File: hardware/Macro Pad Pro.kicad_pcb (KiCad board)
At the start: 2 copper layers, 107 x 134 mm, 149 parts, among them J1 USB_C, J2 Conn_02x08_Odd_Even, J4 Conn_02x01, SW1 SW_Push_B, SW2 SW_Push_R, U1 RP2040, U2 OLED, U3 AP2112K-3.3, U4 USBLC6-2SC6, U6 W25Q128JVS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

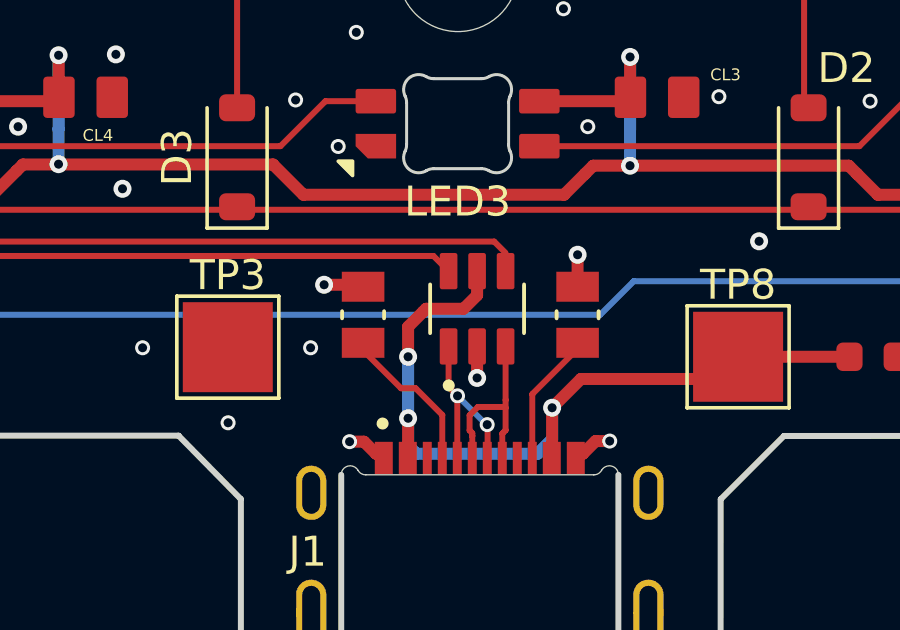
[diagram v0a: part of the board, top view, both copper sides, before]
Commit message: Fixed ERC component footprint
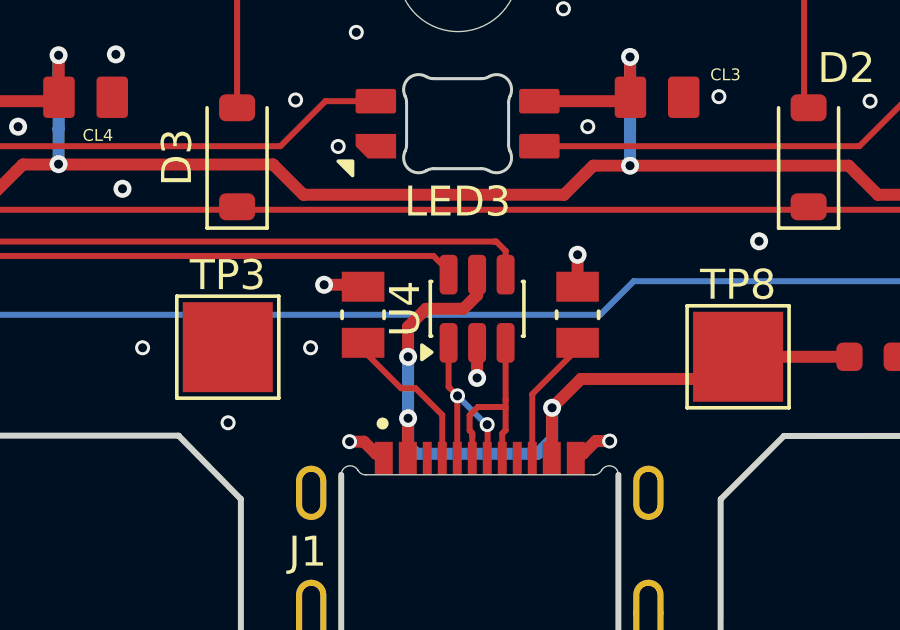
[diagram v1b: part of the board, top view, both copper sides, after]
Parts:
- U4: footprint Personal:SOT95P280X145-6N -> Package_TO_SOT_SMD:SOT-23-6
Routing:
- net ESD_DP: track 131.1 -> 131.9 mm
